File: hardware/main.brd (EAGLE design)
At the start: 95.2 x 80.4 mm, 100 parts, among them IC1 MPU-6050, IC2 TB6612FNG, M1 MOTOR_MOUNT_V2, M2 LED_MOUNT, M3 LED_MOUNT, M4 LED_MOUNT, M5 LED_MOUNT, M6 LED_MOUNT, M7 LED_MOUNT, Q7 IRLML2244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

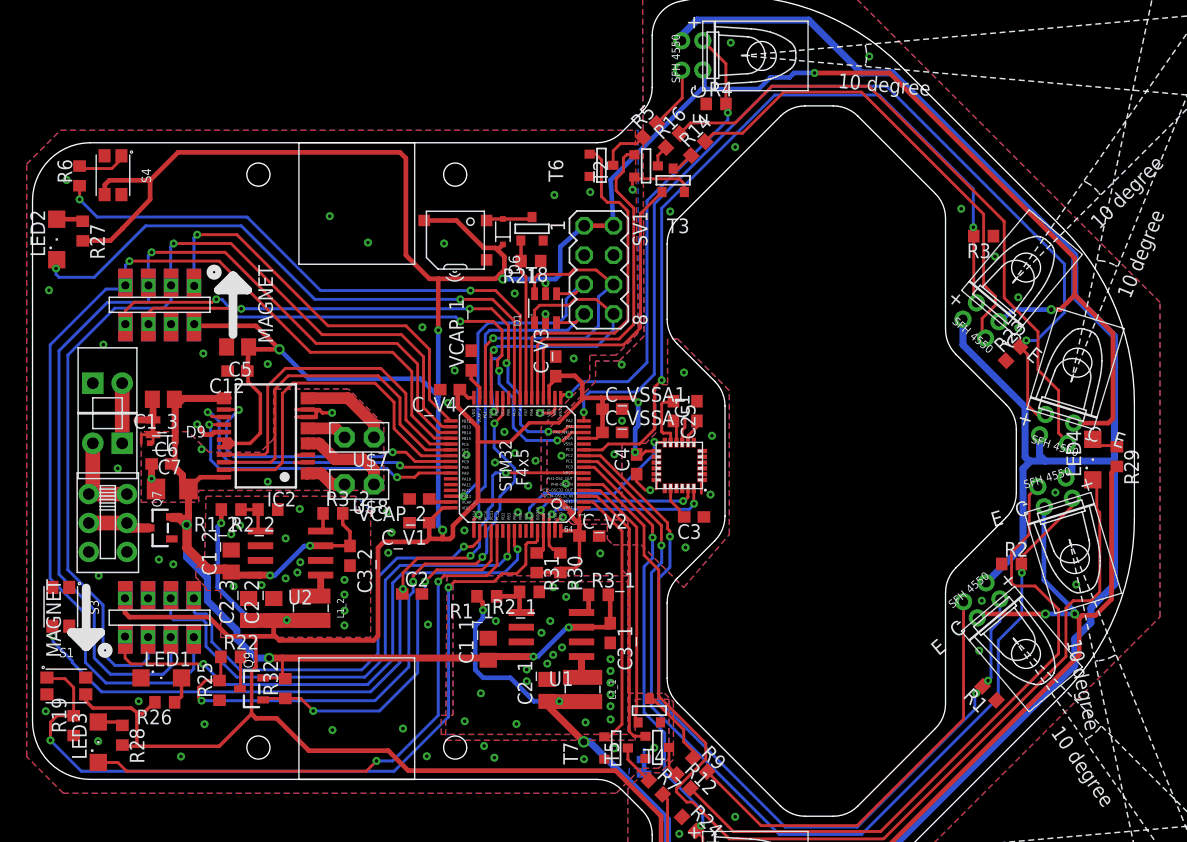
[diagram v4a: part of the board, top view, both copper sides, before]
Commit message: dodanie napisow, odsuniecie kilku sciezek od krawedzi plytki, minimlne zmniejszenie otworu z przodu (aby nie bylo problemu z odlegloscia od krawedzi)
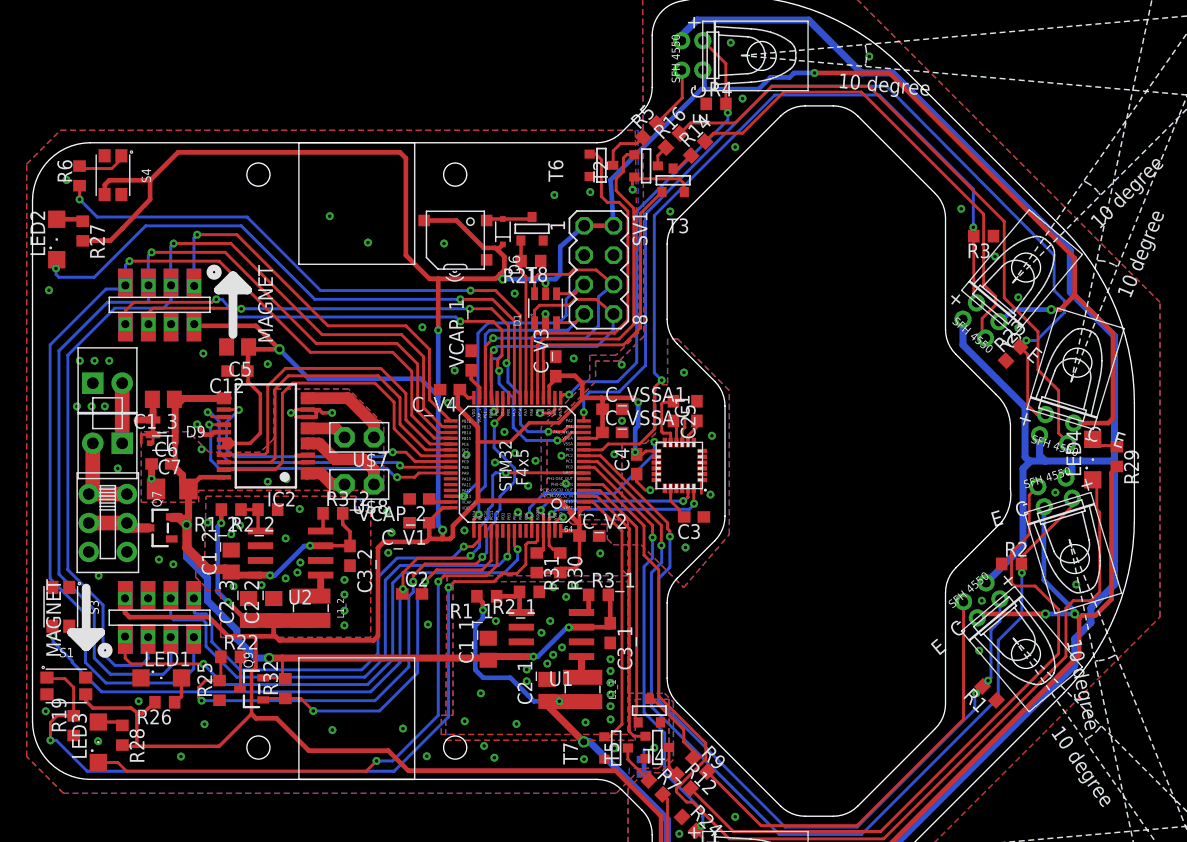
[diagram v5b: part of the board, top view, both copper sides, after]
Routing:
- net +3V3: track 518.3 -> 516.0 mm
- net ADC_LS: track 86.1 -> 85.2 mm
- net N$26: track 0.80 -> 0.00 mm
- net ADC_L: track 70.4 -> 70.9 mm
- net ADC_LF: track 40.4 -> 39.9 mm
- net GNDA: vias 4 -> 6
- net GND: vias 90 -> 96
- net AGND: vias 23 -> 24
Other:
- outline, holes or cut-outs redrawn
- board text added: "2017"
- board text added: "Dixi"
- board text added: "K.Dworakowaski"
- board text added: "K.Trzcinski"
- board text added: "PL"

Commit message: poukladanie warstwy opisowej, dodanie przelotek - wersja finalna
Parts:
- R26, R27, R28: value 150R -> 300R
- R29: value 33R -> 300R
- R32: value (none) -> 10k
- moved ON 0.51 mm to (4.86, -7.13)
- moved R3 0.51 mm to (82.2, 19.9)
- moved JP2 0.38 mm to (5.21, 7.11)
- moved JP1 0.25 mm to (7.75, 1.79)
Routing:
- net ML_IN1: track 30.2 -> 29.5 mm
- net N$46: track 7.83 -> 8.52 mm
- net ML_PWM: track 30.1 -> 29.5 mm
- net ML_IN2: track 30.0 -> 29.5 mm
- net GNDA: vias 6 -> 10
- net GND: vias 96 -> 111

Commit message: dodanie wartosci elementow
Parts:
- R1_1, R1_2, R22: value (none) -> 10k
- R25, R2_2: value (none) -> 15k
- R2_1: value (none) -> 31k
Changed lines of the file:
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@@
 <attribute name="VALUE" x="43.688" y="19.177" size="1.27" layer="27" rot="R180"/>
 </element>
-<element name="R22" library="resistor" package="R0603" value="" x="17.1196" y="-16.9164" smashed="yes">
+<element name="R22" library="resistor" package="R0603" value="10k" x="17.1196" y="-16.9164" smashed="yes">
 <attribute name="NAME" x="15.4686" y="-15.9004" size="1.27" layer="25"/>
 <attribute name="VALUE" x="16.4846" y="-18.8214" size="1.27" layer="27"/>
@@
 <attribute name="VALUE" x="54.922146875" y="-32.241625" size="1.27" layer="27" rot="R315"/>
 </element>
-<element name="R25" library="resistor" package="R0603" value="" x="16.1544" y="-19.812" smashed="yes" rot="R90">
+<element name="R25" library="resistor" package="R0603" value="15k" x="16.1544" y="-19.812" smashed="yes" rot="R90">
 <attribute name="NAME" x="15.2654" y="-21.844" size="1.27" layer="25" rot="R90"/>
 <attribute name="VALUE" x="18.0594" y="-20.447" size="1.27" layer="27" rot="R90"/>
 </element>
-<element name="R1_2" library="rcl" package="R0603" value="" x="17.161" y="-4.191" smashed="yes" rot="R180">
+<element name="R1_2" library="rcl" package="R0603" value="10k" x="17.161" y="-4.191" smashed="yes" rot="R180">
 <attribute name="NAME" x="18.939" y="-2.159" size="1.27" layer="25" rot="R180"/>
 <attribute name="VALUE" x="17.796" y="-2.286" size="1.27" layer="27" rot="R180"/>
 </element>
-<element name="R2_2" library="rcl" package="R0603" value="" x="20.336" y="-4.191" smashed="yes" rot="R180">
+<element name="R2_2" library="rcl" package="R0603" value="15k" x="20.336" y="-4.191" smashed="yes" rot="R180">
 <attribute name="NAME" x="22.876" y="-2.159" size="1.27" layer="25" rot="R180"/>
 <attribute name="VALUE" x="20.971" y="-2.286" size="1.27" layer="27" rot="R180"/>
 </element>
-<element name="R1_1" library="rcl" package="R0603" value="" x="39.243" y="-11.684" smashed="yes" rot="R180">
+<element name="R1_1" library="rcl" package="R0603" value="10k" x="39.243" y="-11.684" smashed="yes" rot="R180">
 <attribute name="NAME" x="38.862" y="-8.763" size="1.27" layer="25" rot="R180"/>
 <attribute name="VALUE" x="39.878" y="-9.779" size="1.27" layer="27" rot="R180"/>
 </element>
-<element name="R2_1" library="rcl" package="R0603" value="" x="42.926" y="-11.303" smashed="yes" rot="R180">
+<element name="R2_1" library="rcl" package="R0603" value="31k" x="42.926" y="-11.303" smashed="yes" rot="R180">
 <attribute name="NAME" x="42.799" y="-8.763" size="1.27" layer="25" rot="R180"/>
 <attribute name="VALUE" x="43.561" y="-9.398" size="1.27" layer="27" rot="R180"/>

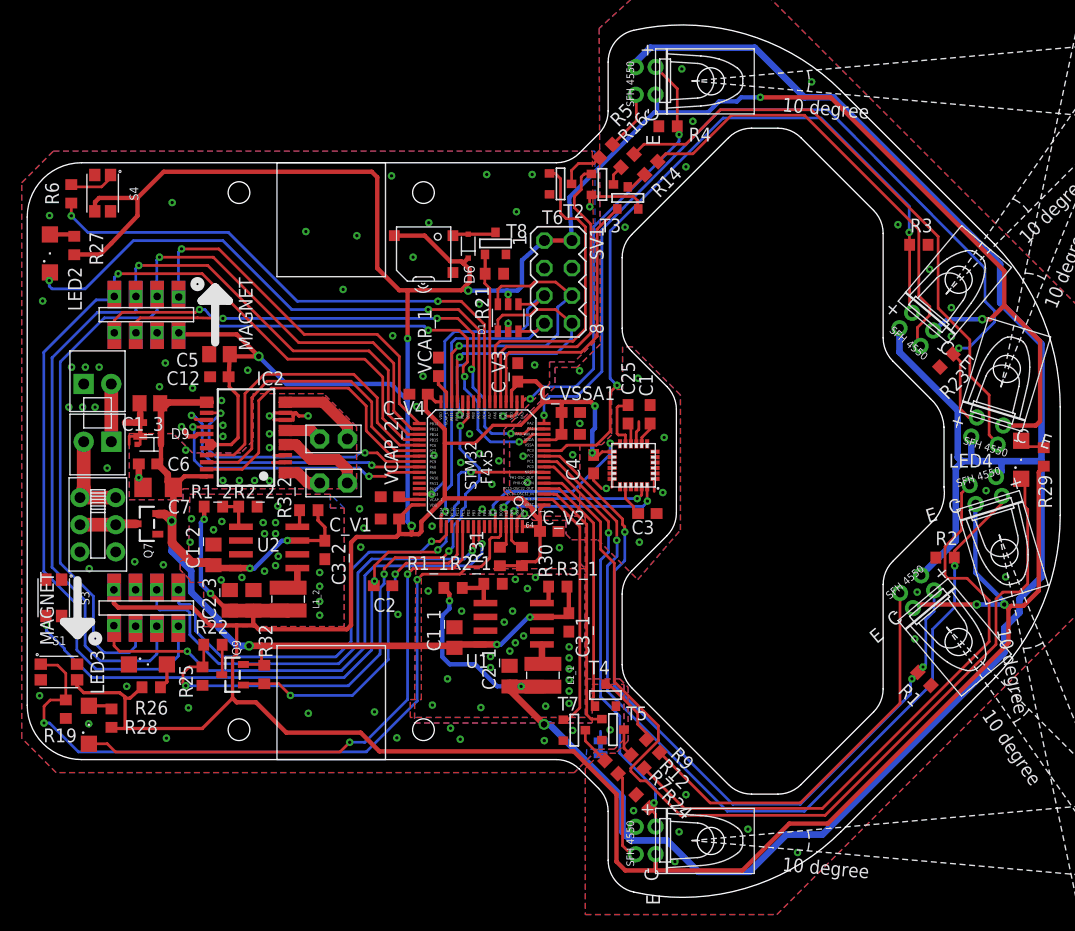
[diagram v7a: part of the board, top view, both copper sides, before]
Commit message: gyro vlogic fixed
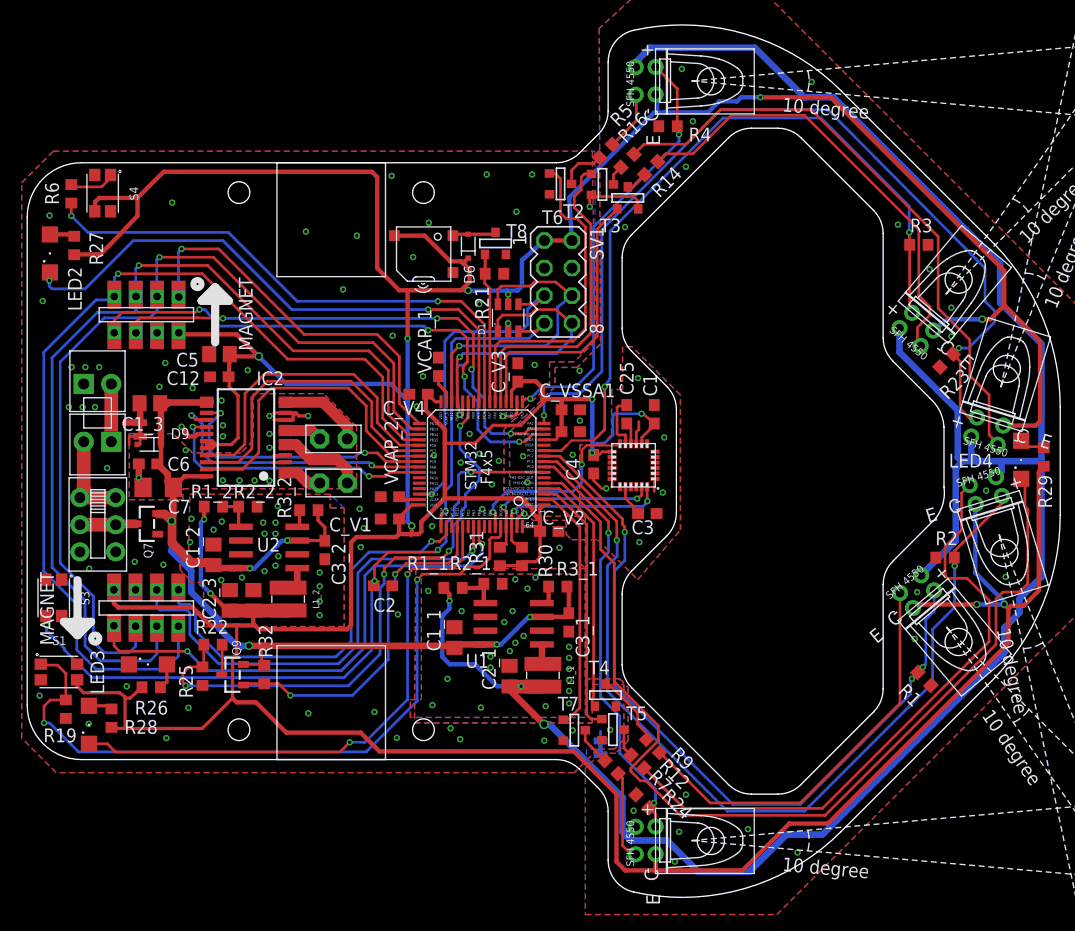
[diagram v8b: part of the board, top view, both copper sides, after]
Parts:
- moved C1 0.38 mm to (57.8, 4.32)
- moved C_VSSA1 0.25 mm to (50.1, 4.74)
- moved C_VSSA 0.25 mm to (50.1, 2.72)
- moved C25 0.13 mm to (55.2, 4.32)
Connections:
- removed net N$34: C1.1, IC1.8
- net +3V3: now also C1.1, IC1.8
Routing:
- net +3V3: track 515.8 -> 527.2 mm, vias 13 -> 14
- net N$34: track 2.19 -> 0.00 mm
- net MPU_INT: track 16.7 -> 17.9 mm
- net ADC_L: track 70.9 -> 70.0 mm
